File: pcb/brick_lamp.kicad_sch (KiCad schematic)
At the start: 11 parts, among them J1 LED_24V_OUT, J2 24V_IN, J3 DEBUG, J4 DEBUG, Q1 CSD17302Q5A, U2 MCP1799x-330xxTT, U3 ATtiny85V-10S

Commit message: Cleanup the layout and schematic
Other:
- moved on the sheet: C1, C2, J1, J2, J3, J4, Q1, R2, R3, U2, U3

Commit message: Fill in schematic sheet details
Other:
- title: (none) -> ATTiny85 24V LED Dimmer
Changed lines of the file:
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@@
 	(generator_version "9.0")
 	(paper "A5")
+	(title_block
+		(title "ATTiny85 24V LED Dimmer")
+		(date "2025-10-17")
+		(rev "1")
+	)
 	(junction
 		(at 74.93 29.21)

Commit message: Cleanup schematics
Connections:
- net PB4: now also J4.4 (Pin_4); no longer J4.2 (Pin_2)
- net PB5: now also J4.2 (Pin_2); no longer J4.4 (Pin_4)
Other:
- moved on the sheet: C1, C2, J1, J2, J3, J4, Q1, R2, R3, U2, U3

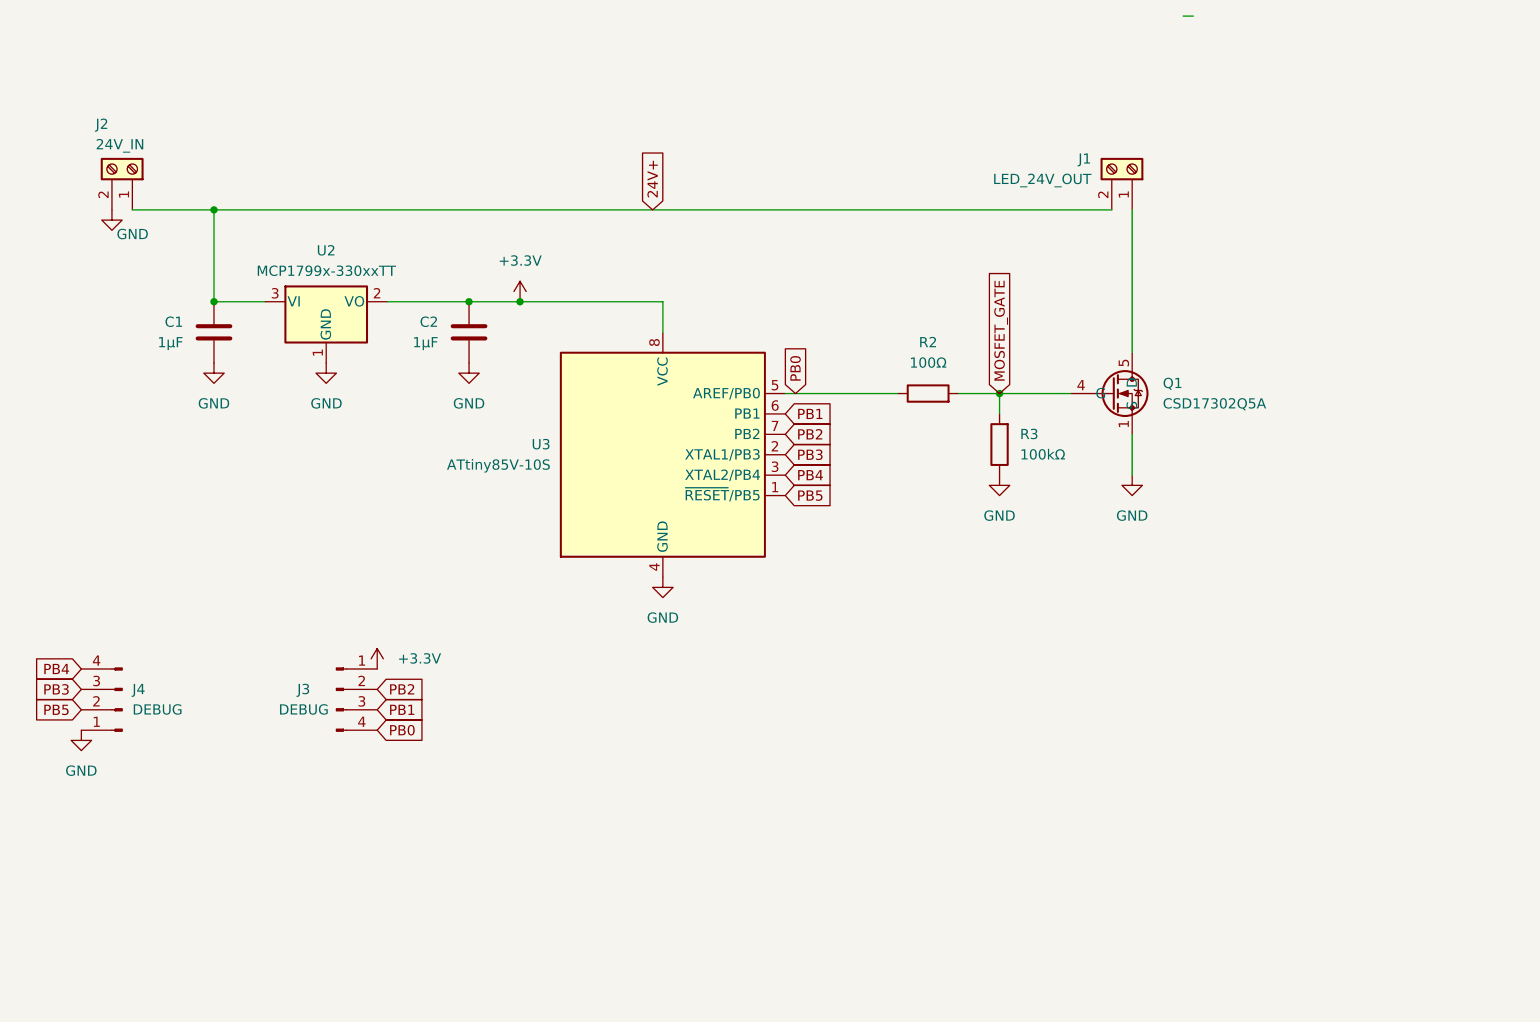
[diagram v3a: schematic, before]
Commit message: Add name of the board to silkscreen; improve current capacity
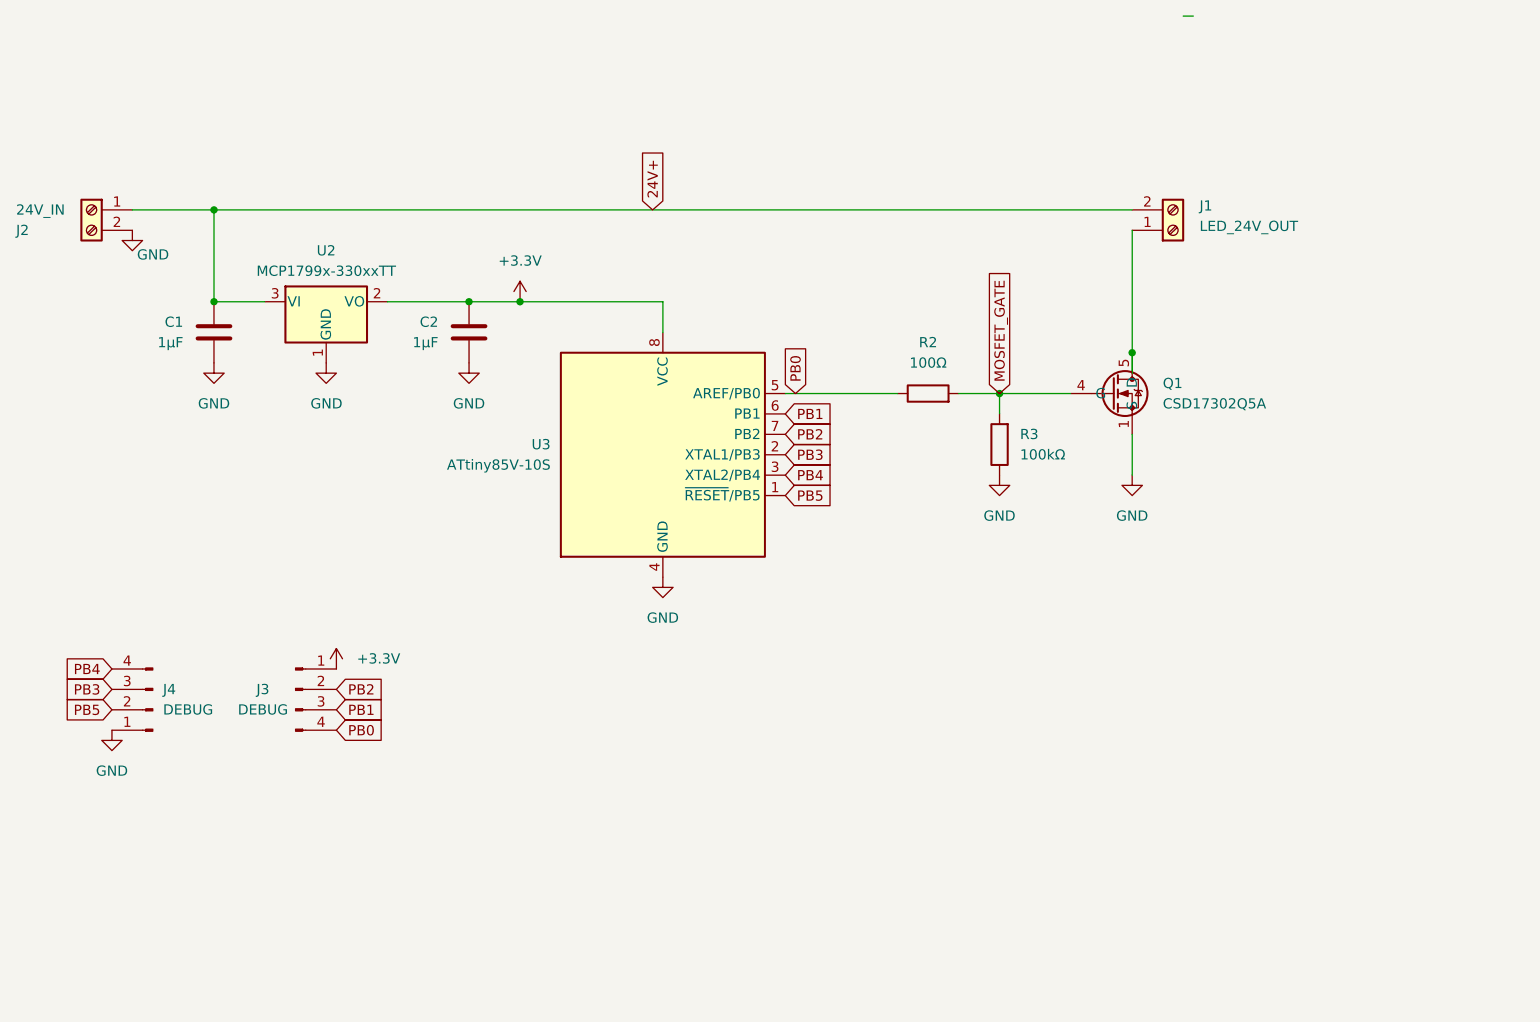
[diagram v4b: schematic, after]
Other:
- moved on the sheet: J1, J2, J3, J4
